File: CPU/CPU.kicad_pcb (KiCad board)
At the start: 2 copper layers, 157.1 x 85.3 mm, 123 parts, among them IC5 MAX803, J101 Conn_02x10_Odd_Even, J102 Conn_01x07_Female, J201 Conn_02x03_Odd_Even, J302 1X4SMD-FPC, J303 Conn_02x03_Odd_Even, Q101 IRLML0040TR, Q102 IRLML0040TR, Q201 DMC4050, Q202 IRLML0040TR, Q301 IRLML0040TR, Q401 IRLML0040TR, SW101 SW_SPDT, SW201 TACTILE_SWITCHPTS540-SMD, SW202 TACTILE_SWITCHPTS540-SMD, SW203 TACTILE_SWITCHPTS540-SMD, SW204 TACTILE_SWITCHPTS540-SMD, SW205 TACTILE_SWITCHPTS540-SMD, SW206 TACTILE_SWITCHPTS540-SMD, SW207 TACTILE_SWITCHPTS540-SMD, SW208 TACTILE_SWITCHPTS540-SMD, SW209 TACTILE_SWITCHPTS540-SMD, SW210 TACTILE_SWITCHPTS540-SMD, SW211 TACTILE_SWITCHPTS540-SMD, SW212 TACTILE_SWITCHPTS540-SMD, SW213 TACTILE_SWITCHPTS540-SMD, U1 CAT24C32, U101 LP2989-3.3_SOIC8_VSSOP8, U201 ATmega328PB-AU, U301 OPT3001, U302 ATtiny1614-SS, X1 DISP_LCD_3.5IN_320X480_50PIN, Y201 Resonator_Small

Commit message: BuyDisplay LCD.
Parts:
- removed C101, C103: 10uF, Capacitor_SMD:C_0805_2012Metric_Pad1.15x1.40mm_HandSolder
- removed C102: 0.1uF, Capacitor_SMD:C_0805_2012Metric_Pad1.15x1.40mm_HandSolder
- removed IC5: MAX803, PiTFT:SOT23
- removed R105: 100K, Resistor_SMD:R_0805_2012Metric_Pad1.15x1.40mm_HandSolder
- removed R12, R13, R14: 3.9K, Resistor_SMD:R_0805_2012Metric_Pad1.15x1.40mm_HandSolder
- removed R6: 10K, Resistor_SMD:R_0805_2012Metric_Pad1.15x1.40mm_HandSolder
- removed SJ1, SJ101, SJ2: SOLDERJUMPERCLOSED, PiTFT:SOLDERJUMPER_CLOSEDWIRE
- removed U1: CAT24C32, PiTFT:SOIC8_150MIL
- removed U101: LP2989-3.3_SOIC8_VSSOP8, Package_SO:TSSOP-8_3x3mm_P0.65mm
- added R401: 10, Resistor_SMD:R_0805_2012Metric_Pad1.15x1.40mm_HandSolder, B.Cu at (80.5, 97.0)
- moved C4 37.3 mm to (82.5, 102.5), turned to 0 degrees
- moved C1 35.2 mm to (82.5, 100.0)
- moved R5 14.0 mm to (82.0, 74.0), turned to 180 degrees
- moved TP103 8.16 mm to (129.0, 48.0)
- moved TP102 7.11 mm to (135.5, 48.0)
- moved R3 6.06 mm to (82.2, 80.0)
- moved R4 6.03 mm to (82.2, 77.5)
- moved Q401 0.75 mm to (80.0, 94.0)
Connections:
- Pi101 pad 16: /LCD_BACK_LIGHT -> Net-(Pi101-Pad16)
- Pi101 pad 22: /TFT_DC -> Net-(Pi101-Pad22)
- Pi101 pad 27: /EEDATA -> /TFT_RST
- Pi101 pad 28: /EECLK -> /TFT_DC
- Pi101 pad 29: Net-(Pi101-Pad29) -> /LCD_BACK_LIGHT
- Pi101 pad 3: Net-(Pi101-Pad3) -> /SDA
- Pi101 pad 5: Net-(Pi101-Pad5) -> /SCL
- X1 pad 1: +3V3 -> Net-(R401-Pad1)
- X1 pad 10: /Display/TFT_RST -> /TFT_RST
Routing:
- net /TFT_DC: track 0.00 -> 75.7 mm
- net /TFT_RST: track 0.00 -> 72.5 mm
- net +3V3: track 519.7 -> 459.7 mm, vias 10 -> 5
- net /LCD_BACK_LIGHT: track 12.0 -> 65.2 mm
- net /EECLK: track 45.8 -> 0.00 mm
- net /EEDATA: track 45.5 -> 0.00 mm
- net /Pi5V: track 130.3 -> 92.8 mm
- net /Display/TFT_RST: track 35.2 -> 0.00 mm
- net /TFT_CS: track 58.1 -> 72.2 mm, vias 2 -> 0
- net /MOSI: track 66.8 -> 80.0 mm, vias 2 -> 0
- net /SCLK: track 77.4 -> 68.2 mm, vias 4 -> 0
- net /PiTX: track 42.6 -> 33.6 mm, vias 3 -> 1
- net GND: track 6.72 -> 15.2 mm, vias 290 -> 321
- net Net-(R14-Pad1): track 7.07 -> 0.00 mm
- net /SDA: track 159.6 -> 166.3 mm
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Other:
- board text added: "TAPE"

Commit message: Update.
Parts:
- removed Q301: IRLML0040TR, CPU:SOT23
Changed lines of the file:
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@@
     (tracks 1940)
     (zones 0)
-    (modules 110)
+    (modules 109)
     (nets 117)
   )
@@
     (44 Edge.Cuts user)
     (45 Margin user hide)
-    (46 B.CrtYd user hide)
+    (46 B.CrtYd user)
     (47 F.CrtYd user hide)
     (48 B.Fab user hide)
@@
   )
   (setup
-    (last_trace_width 1)
+    (last_trace_width 0.25)
     (user_trace_width 0.4)
     (user_trace_width 0.5)
@@
       (solder_mask_margin 0.1016))
   )
-  (module CPU:SOT23 (layer Bottom)
-    (at 178 53 180)
-    (attr smd)
-    (fp_text reference Q301 (at 1.8 2.5 unlocked) (layer B.SilkS)
-      (effects (font (size 1 1) (thickness 0.15)) (justify right bottom mirror))
-    )
-    (fp_text value IRLML0040TR (at -1.905 -3.175) (layer B.Fab)
-      (effects (font (size 1 1) (thickness 0.15)) (justify left bottom mirror))
-    )
-    (fp_text user 3 (at -1.27 1.27) (layer Cmts.User)
-      (effects (font (size 0.57912 0.57912) (thickness 0.048768)) (justify left bottom))
-    )
-    (fp_text user 2 (at 1.905 -1.27) (layer Cmts.User)
-      (effects (font (size 0.57912 0.57912) (thickness 0.048768)) (justify left bottom))
-    )
-    (fp_text user 1 (at -1.905 -1.27) (layer Cmts.User)
-      (effects (font (size 0.57912 0.57912) (thickness 0.048768)) (justify left bottom))
-    )
-    (fp_poly (pts (xy -1.1684 -1.2954) (xy -0.7112 -1.2954) (xy -0.7112 -0.7112) (xy -1.1684 -0.7112)) (layer B.Fab) (width 0))
-    (fp_poly (pts (xy 0.7112 -1.2954) (xy 1.1684 -1.2954) (xy 1.1684 -0.7112) (xy 0.7112 -0.7112)) (layer B.Fab) (width 0))
-    (fp_poly (pts (xy -0.2286 0.7112) (xy 0.2286 0.7112) (xy 0.2286 1.2954) (xy -0.2286 1.2954)) (layer B.Fab) (width 0))
-    (fp_line (start -1.422 0.66) (end 1.422 0.66) (layer B.Fab) (width 0.1524))
-    (fp_line (start -1.422 -0.66) (end -1.422 0.66) (layer B.Fab) (width 0.1524))
-    (fp_line (start 1.422 -0.66) (end -1.422 -0.66) (layer B.Fab) (width 0.1524))
-    (fp_line (start 1.422 0.66) (end 1.422 -0.66) (layer B.Fab) (width 0.1524))
-    (fp_text user 270 (at 0 0 180) (layer B.Fab)
-      (effects (font (size 1 1) (thickness 0.15)) (justify mirror))
-    )
-    (pad 1 smd rect (at -0.95 -1.1 180) (size 0.6 1.4) (layers Bottom B.Paste B.Mask)
-      (net 61 "/I2C Devices/LED_PWM") (solder_mask_margin 0.1016))
-    (pad 2 smd rect (at 0.95 -1.1 180) (size 0.6 1.4) (layers Bottom B.Paste B.Mask)
-      (net 1 GND) (solder_mask_margin 0.1016))
-    (pad 3 smd rect (at 0 1.1 180) (size 1 1.4) (layers Bottom B.Paste B.Mask)
-      (net 98 "Net-(C304-Pad1)") (solder_mask_margin 0.1016))
-    (model ${KISYS3DMOD}/Package_TO_SOT_SMD.3dshapes/SOT-23.step
-      (at (xyz 0 0 0))
-      (scale (xyz 1 1 1))
-      (rotate (xyz 0 0 -90))
-    )
-  )
   (module CPU:DNP0006A (layer Top)
     (at 58 47.11)
@@
   (segment (start 146.215 71.965) (end 146.55 72.3) (width 0.25) (layer Bottom) (net 5))
   (segment (start 143.045 70.51) (end 144.5 71.965) (width 0.25) (layer Bottom) (net 5))
-  (segment (start 137.22 101) (end 137.23 100.99) (width 0.25) (layer Bottom) (net 15))
   (segment (start 78.494236 75.905764) (end 75.331246 75.905764) (width 0.25) (layer Bottom) (net 13))
   (segment (start 80.975 74) (end 80.4 74) (width 0.25) (layer Bottom) (net 13))
@@
   (segment (start 83.275 77.5) (end 83.85 77.5) (width 0.25) (layer Bottom) (net 14))
   (segment (start 83.85 77.5) (end 103.35 97) (width 0.25) (layer Bottom) (net 14))
+  (segment (start 137.22 101) (end 137.23 100.99) (width 0.25) (layer Bottom) (net 15))
   (segment (start 133.415 99) (end 135.405 100.99) (width 0.25) (layer Bottom) (net 15))
   (segment (start 99.5 99) (end 133.415 99) (width 0.25) (layer Bottom) (net 15))

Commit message: Version 4 of the CPU board ordered with this commit.
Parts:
- added D101: TVS, Diode_SMD:D_SMB-SMC_Universal_Handsoldering, B.Cu at (38.5, 61.5)
- added F101: Polyfuse_Small, Fuse:Fuse_1210_3225Metric_Pad1.42x2.65mm_HandSolder, B.Cu at (40.0, 53.0)
- added Q301: IRLML0040TR, CPU:SOT23, B.Cu at (177.8, 51.9)
- moved C202 5.43 mm to (38.0, 73.5), turned to 90 degrees
- moved C201 2.63 mm to (35.0, 53.5), turned to 0 degrees
- moved R301 1.96 mm to (43.5, 60.7), turned to 90 degrees
- moved C4 1.00 mm to (82.5, 103.5)
- moved C1 0.50 mm to (82.5, 100.5)
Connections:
- J101 pad 1: 5V -> Net-(F101-Pad2)
- J101 pad 11: 5V -> Net-(F101-Pad2)
- J101 pad 13: 5V -> Net-(F101-Pad2)
- J101 pad 3: 5V -> Net-(F101-Pad2)
- J101 pad 5: 5V -> Net-(F101-Pad2)
- J101 pad 7: 5V -> Net-(F101-Pad2)
- J101 pad 9: 5V -> Net-(F101-Pad2)
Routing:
- net Net-(F101-Pad2): track 0.00 -> 24.3 mm
- net 5V: track 531.8 -> 543.9 mm, vias 14 -> 16
- net +3V3: track 459.7 -> 460.9 mm
- net /Micro Controller Devices/SWU: track 150.5 -> 151.4 mm
- net /I2C Devices/LED_PWM: track 38.6 -> 37.8 mm
- net GND: vias 321 -> 324
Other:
- outline, holes or cut-outs redrawn
- board text added: "3V"
- board text added: "CR101 CPU Board V4 mquezada 20200717"
- board text added: "CS"
- board text added: "DC"
- board text added: "LCD_BL"
- board text added: "RST"
- board text added: "SCLK"
- board text removed: "CR101 CPU Board V3 mquezada 20200519"
- board text removed: "LCD interface circuit by Adafruit. Referenced from PiTFT 3.5""

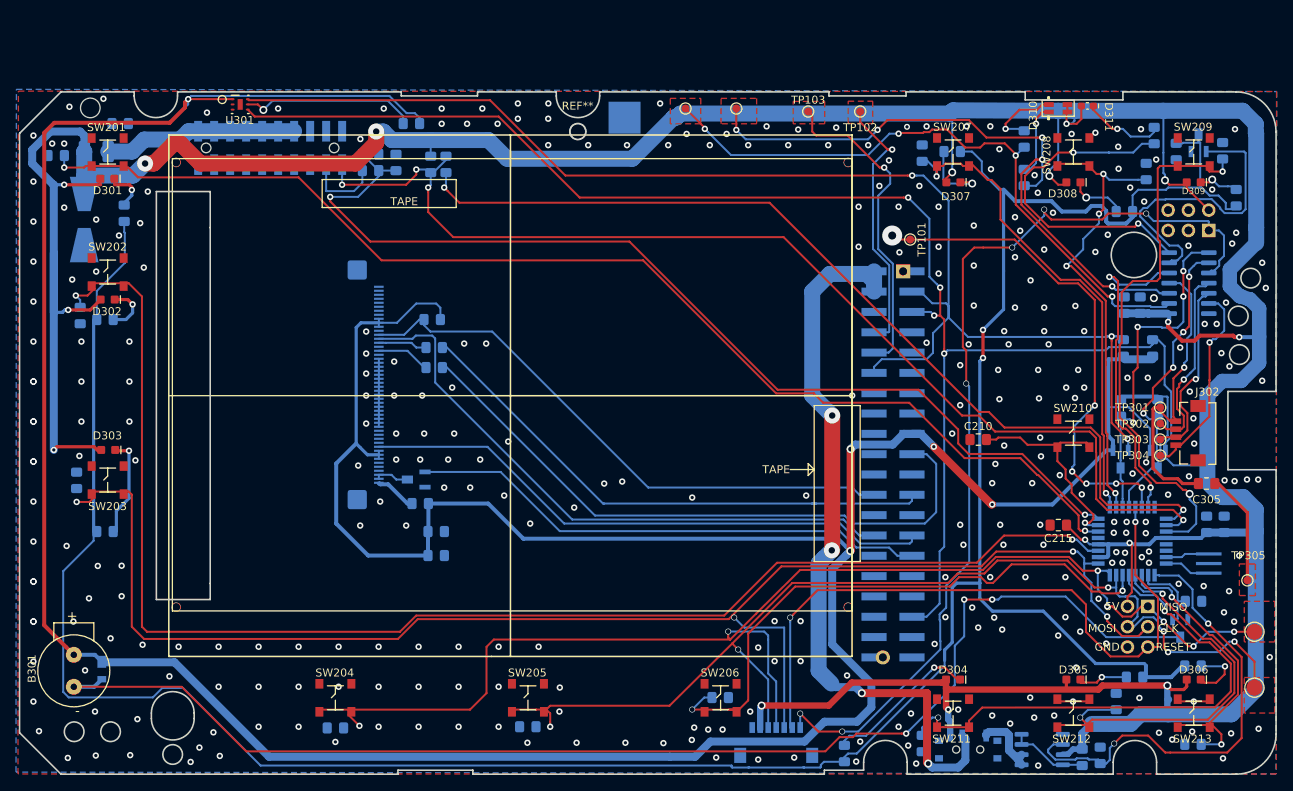
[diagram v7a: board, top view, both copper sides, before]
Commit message: Fix placement of the RPi, prepare for V5.
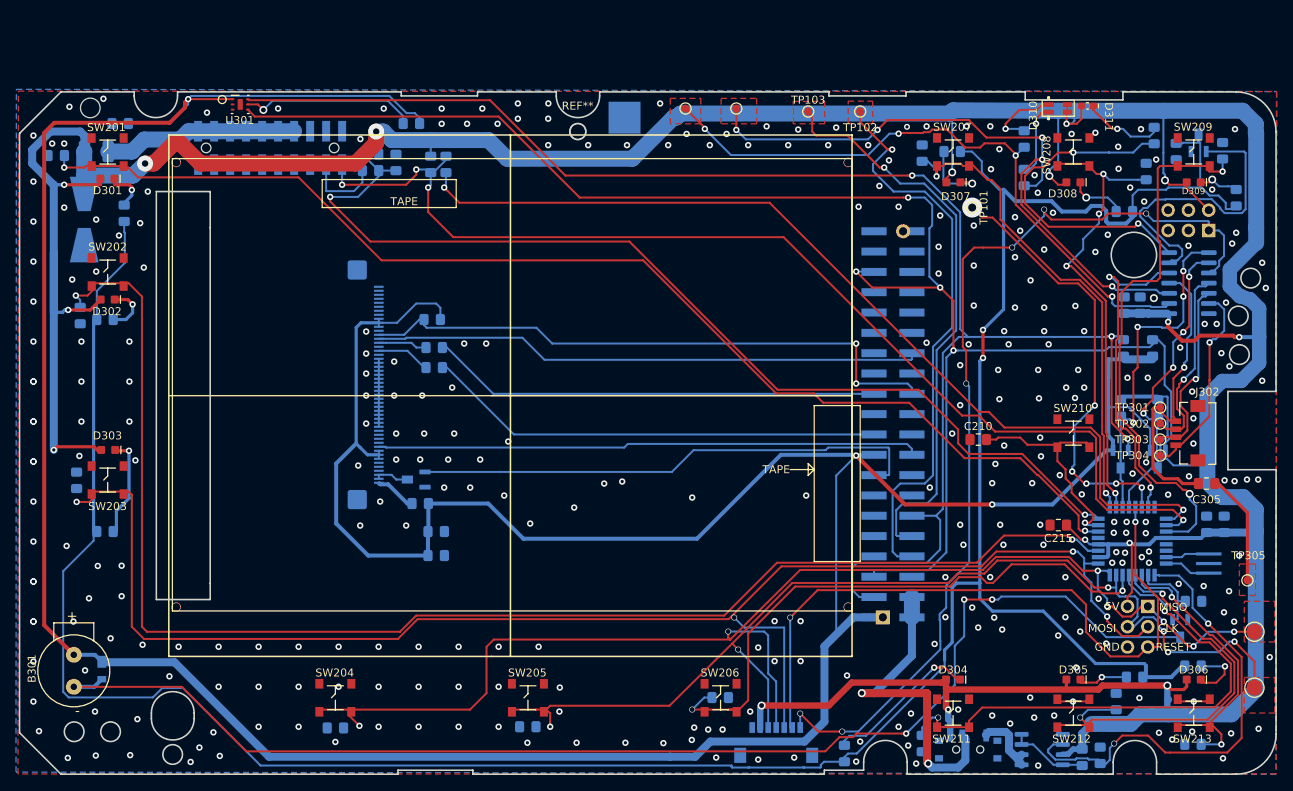
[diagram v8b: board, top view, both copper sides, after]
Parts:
- moved Pi101 80.1 mm to (113.1, 119.6), turned to 90 degrees
- moved TP101 8.72 mm to (149.5, 60.0)
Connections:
- Pi101 pad 1: Net-(Pi101-Pad1) -> +3V3
- Pi101 pad 13: /LCD_PWR -> /RT_INIT
- Pi101 pad 15: Net-(Pi101-Pad15) -> /LCD_BACK_LIGHT
- Pi101 pad 18: /RT_INIT -> /TFT_RST
- Pi101 pad 27: /TFT_RST -> Net-(Pi101-Pad27)
- Pi101 pad 29: /LCD_BACK_LIGHT -> /LCD_PWR
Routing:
- net /Pi5V: track 92.8 -> 41.1 mm, vias 4 -> 2
- net /PiTX: track 33.6 -> 72.3 mm
- net /PiRX: track 40.4 -> 71.9 mm
- net /SDA: track 166.3 -> 195.4 mm
- net /MOSI: track 80.0 -> 57.4 mm
- net /SCLK: track 68.2 -> 56.3 mm
- net /SCL: track 190.4 -> 201.3 mm
- net /PI_RESET_TOGGLE: track 63.8 -> 54.7 mm
- net /TFT_DC: track 75.7 -> 68.6 mm
- net /TFT_RST: track 72.5 -> 67.9 mm
- net +3V3: track 460.9 -> 464.7 mm, vias 5 -> 3
- net /TFT_CS: track 72.2 -> 75.0 mm, vias 0 -> 2
- net GND: track 15.2 -> 16.3 mm, vias 324 -> 321
- net /LCD_BACK_LIGHT: track 65.2 -> 64.5 mm
